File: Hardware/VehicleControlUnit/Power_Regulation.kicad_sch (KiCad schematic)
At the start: 8 parts

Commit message: ughhhhhhhhhhhhhhhhhhh VCU will lokwey explode and propell the car
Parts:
- removed F4, F5: Polyfuse, symbol Device:Polyfuse
- renumbered F6 to F4, R43 to R50, R44 to R51, R45 to R52
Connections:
- net Power_Mux/VIN_2 is gone; now on net +V_USB: R51.1
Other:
- moved on the sheet: F4, R51, R52

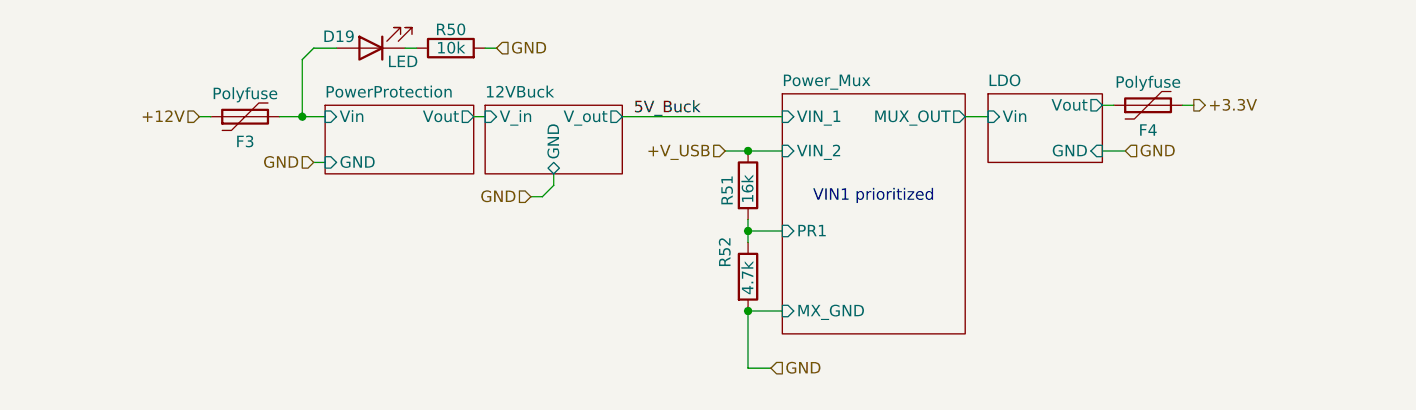
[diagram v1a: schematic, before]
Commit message: need to update design blocks
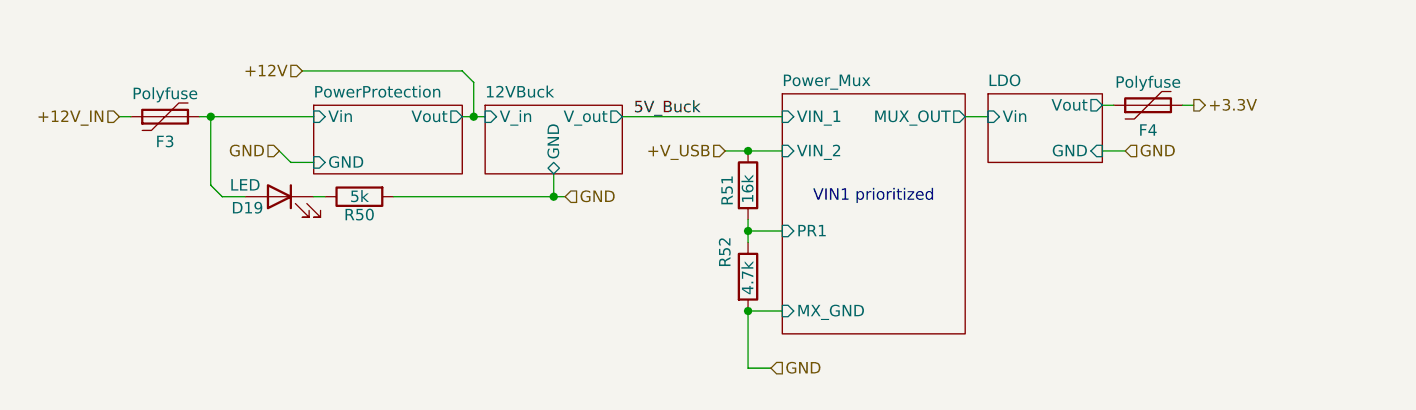
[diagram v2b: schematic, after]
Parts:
- R50: value 10k -> 5k
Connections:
- net +12V: no longer F3.1
- new net +12V_IN: F3.1
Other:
- moved on the sheet: D19, F3, R50

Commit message: pre layout
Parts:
- removed F3: Polyfuse, symbol Device:Polyfuse
- added F3: Fuse, symbol Device:Fuse
- D19: footprint (none) -> LED_SMD:LED_0603_1608Metric
- R51: renamed from R50; footprint (none) -> Resistor_SMD:R_0603_1608Metric_Pad0.98x0.95mm_HandSolder
- R52: renamed from R51; footprint (none) -> Resistor_SMD:R_0603_1608Metric_Pad0.98x0.95mm_HandSolder
- R53: renamed from R52; footprint (none) -> Resistor_SMD:R_0603_1608Metric_Pad0.98x0.95mm_HandSolder
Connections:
- net +12V_IN: now also F3.1
- net PowerProtection/Vin: now also F3.2

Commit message: stoopid lck files
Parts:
- removed F4: Polyfuse, symbol Device:Polyfuse
- F1: renamed from F3; footprint (none) -> FuseHolder:FUSE_3568
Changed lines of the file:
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@@
 	(wire
 		(pts
-			(xy 144.78 50.8) (xy 143.51 50.8)
+			(xy 143.51 50.8) (xy 146.05 50.8)
 		)
 		(stroke
@@
 		(pts
 			(xy 64.77 60.96) (xy 82.55 60.96)
-		)
-		(stroke
-			(width 0)
-			(type default)
-		)
-	)
-	(wire
-		(pts
-			(xy 153.67 50.8) (xy 152.4 50.8)
 		)
 		(stroke
@@
 	(hierarchical_label "+3.3V"
 		(shape output)
-		(at 153.67 50.8 0)
+		(at 146.05 50.8 0)
 		(effects
 			(font
@@
 			)
 			(justify right)
-		)
-	)
-	(symbol
-		(lib_id "Device:Polyfuse")
-		(at 148.59 50.8 90)
-		(unit 1)
-		(body_style 1)
-		(exclude_from_sim no)
-		(in_bom yes)
-		(on_board yes)
-		(in_pos_files yes)
-		(dnp no)
-		(property "Reference" "F4"
-			(at 148.59 53.594 90)
-			(show_name no)
-			(do_not_autoplace no)
-			(effects
-				(font
-					(size 1.27 1.27)
-				)
-			)
-		)
-		(property "Value" "Polyfuse"
-			(at 148.59 48.26 90)
-			(show_name no)
-			(do_not_autoplace no)
-			(effects
-				(font
-					(size 1.27 1.27)
-				)
-			)
-		)
-		(property "Footprint" ""
-			(at 153.67 49.53 0)
-			(hide yes)
-			(show_name no)
-			(do_not_autoplace no)
-			(effects
-				(font
-					(size 1.27 1.27)
-				)
-				(justify left)
-			)
-		)
-		(property "Datasheet" ""
-			(at 148.59 50.8 0)
-			(hide yes)
-			(show_name no)
-			(do_not_autoplace no)
-			(effects
-				(font
-					(size 1.27 1.27)
-				)
-			)
-		)
-		(property "Description" "Resettable fuse, polymeric positive temperature coefficient"
-			(at 148.59 50.8 0)
-			(hide yes)
-			(show_name no)
-			(do_not_autoplace no)
-			(effects
-				(font
-					(size 1.27 1.27)
-				)
-			)
-		)
-		(pin "2"
-		)
-		(pin "1"
-		)
-		(instances
-			(project "VehicleControlUnit"
-				(path "/e864fac9-3897-46c9-9101-6d5488c6cd3a/f16a8bc3-f058-4d27-badd-0afc148d009e"
-					(reference "F4")
-					(unit 1)
-				)
-			)
 		)
 	)
@@
 		(in_pos_files yes)
 		(dnp no)
-		(property "Reference" "F3"
+		(property "Reference" "F1"
 			(at 39.37 46.99 90)
 			(show_name no)
@@
 			)
 		)
-		(property "Footprint" ""
+		(property "Footprint" "FuseHolder:FUSE_3568"
 			(at 39.37 53.848 90)
 			(hide yes)
@@
 			(project "VehicleControlUnit"
 				(path "/e864fac9-3897-46c9-9101-6d5488c6cd3a/f16a8bc3-f058-4d27-badd-0afc148d009e"
-					(reference "F3")
+					(reference "F1")
 					(unit 1)
 				)
